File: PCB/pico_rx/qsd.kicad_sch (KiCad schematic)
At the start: 18 parts

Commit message: Update memory files, Update schematic
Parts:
- C? (x4): value 27n -> 15n
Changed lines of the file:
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@@
       (effects (font (size 1.27 1.27)))
     )
-    (property "Value" "27n" (at 176.276 143.51 90)
+    (property "Value" "15n" (at 176.276 143.51 90)
       (effects (font (size 1.27 1.27)))
     )
@@
       (effects (font (size 1.27 1.27)))
     )
-    (property "Value" "27n" (at 176.276 104.14 90)
+    (property "Value" "15n" (at 176.276 104.14 90)
       (effects (font (size 1.27 1.27)))
     )
@@
       (effects (font (size 1.27 1.27)))
     )
-    (property "Value" "27n" (at 166.116 143.51 90)
+    (property "Value" "15n" (at 166.116 143.51 90)
       (effects (font (size 1.27 1.27)))
     )
@@
       (effects (font (size 1.27 1.27)))
     )
-    (property "Value" "27n" (at 166.116 104.14 90)
-      (effects (font (size 1.27 1.27)))
-    )
+    (property "Value" "15n" (at 166.116 104.14 90)
+      (effects (font (size 1.27 1.27)))
+    )

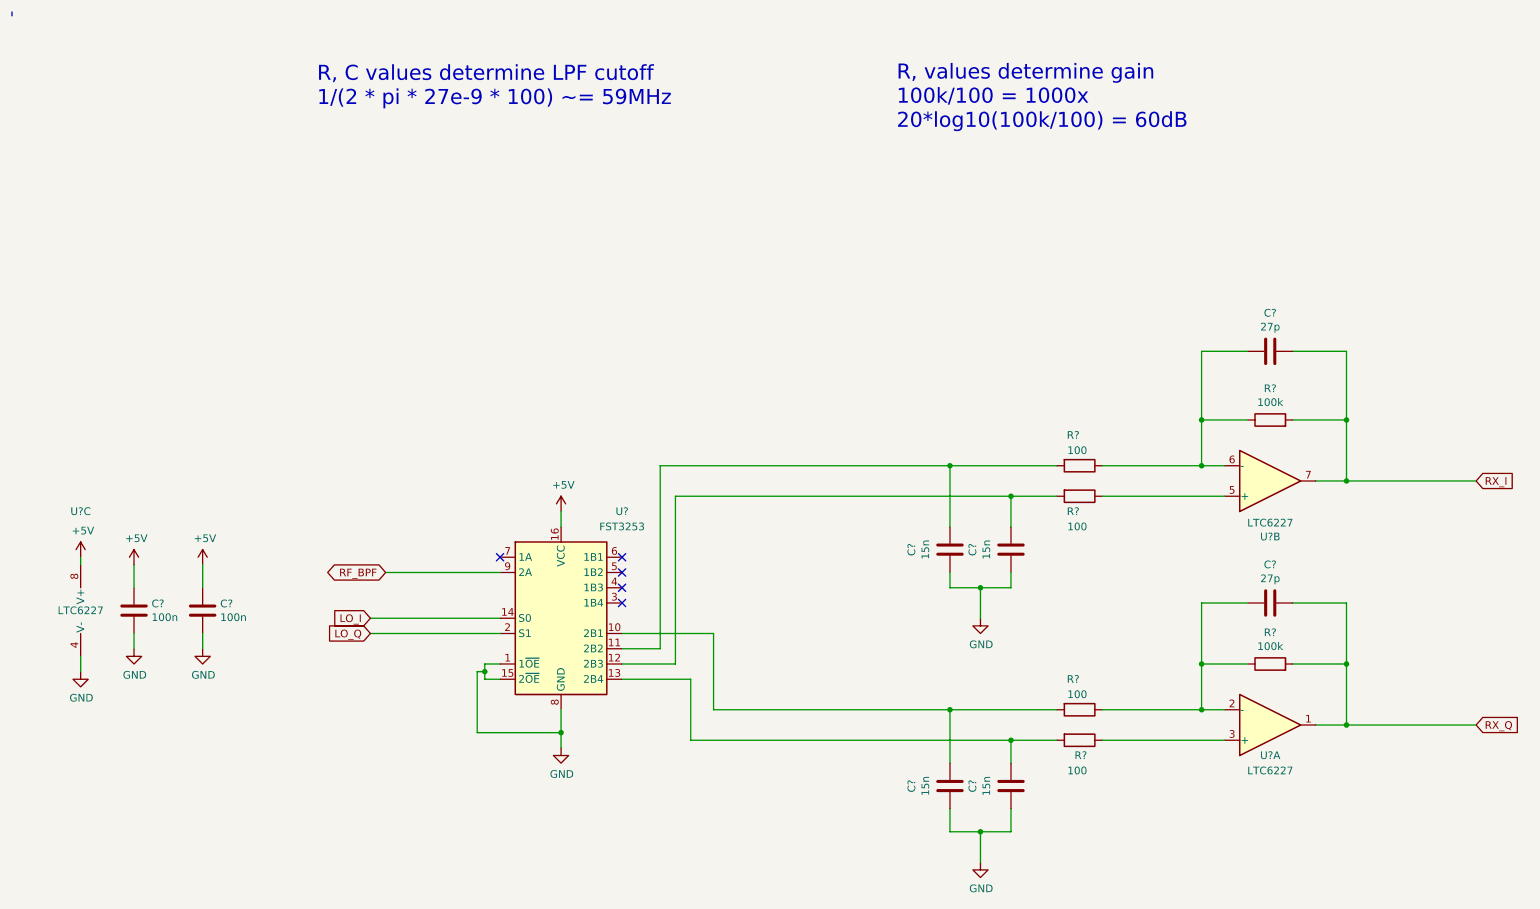
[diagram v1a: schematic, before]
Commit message: Correct error in schematic
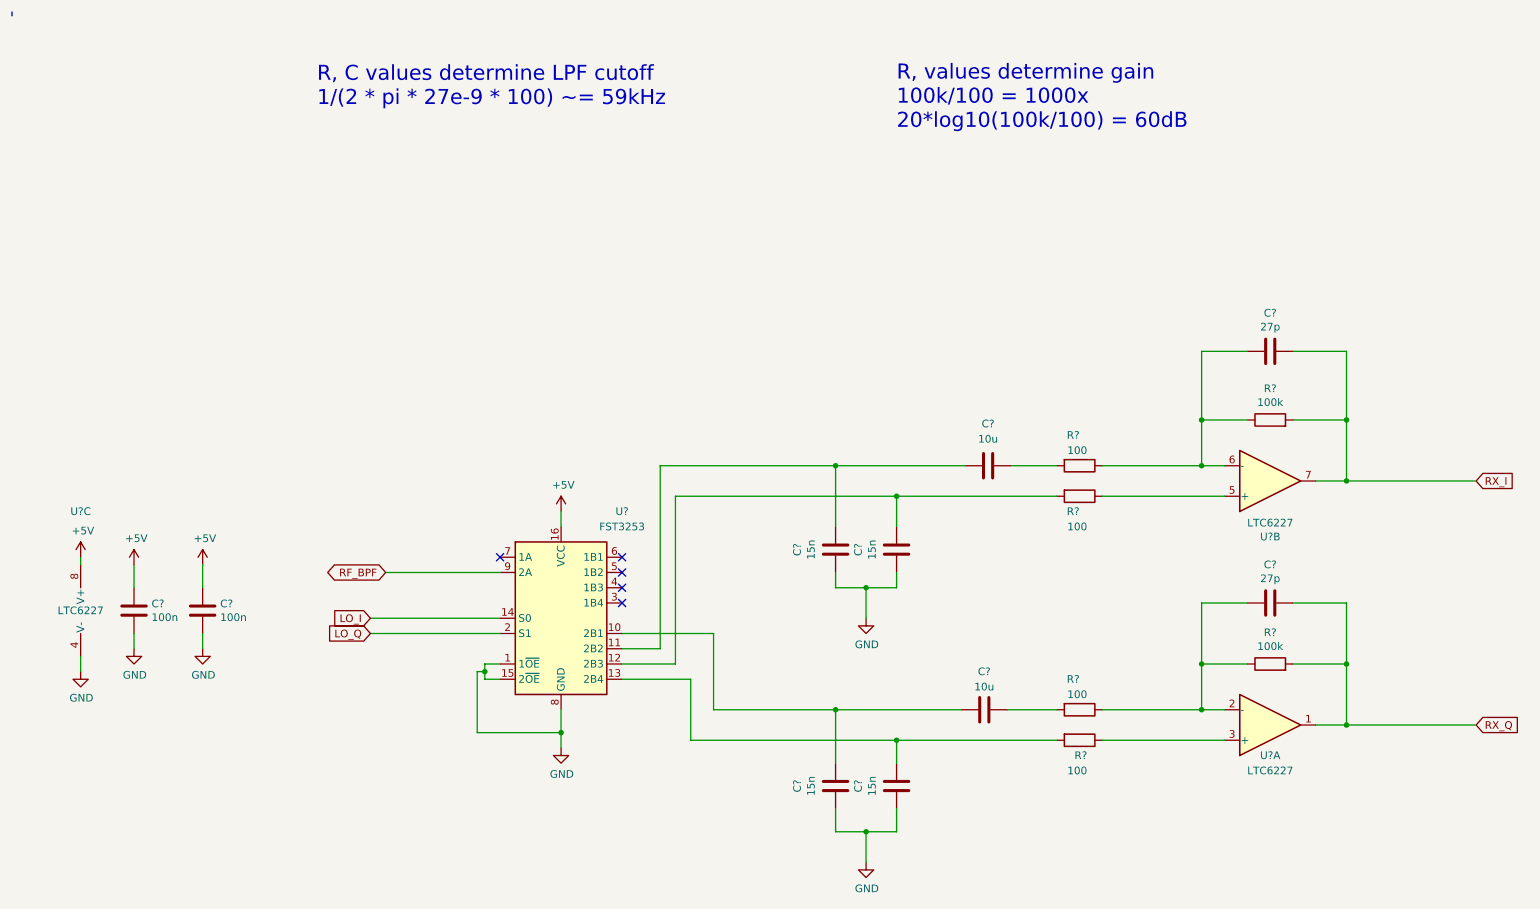
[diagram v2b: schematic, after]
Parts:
- added C? (x2): 10u, Capacitor_SMD:C_0805_2012Metric, symbol Device:C
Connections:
- net at C?.2, U?.10 (2B1): now also C?.2; no longer R?.2
- net at C?.2, U?.11 (2B2): now also C?.2; no longer R?.2
- new net: C?.1, R?.2 (x2)
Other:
- note added: "R, C values determine LPF cutoff 1/(2 * pi * 27e-9 * 100) ~= 59kHz"
- note removed: "R, C values determine LPF cutoff 1/(2 * pi * 27e-9 * 100) ~= 59MHz"
- moved on the sheet: C?

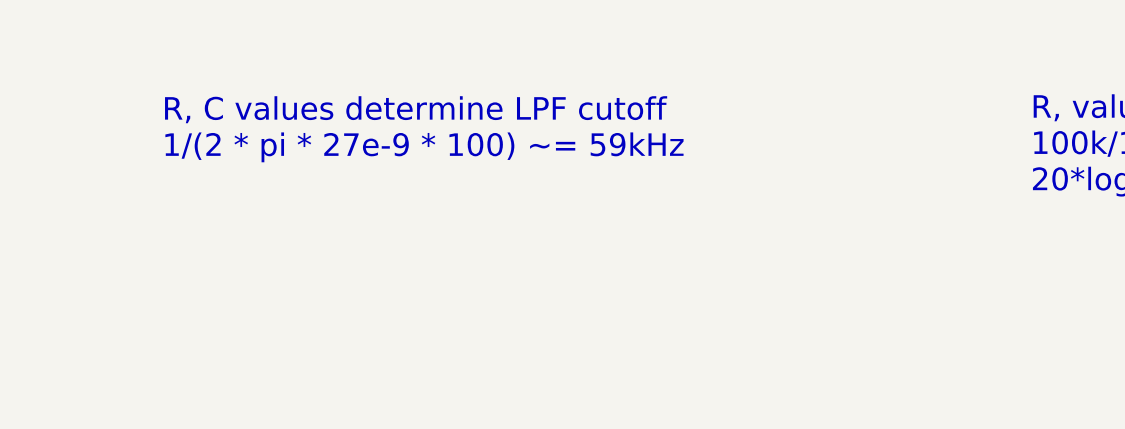
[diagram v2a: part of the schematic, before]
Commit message: Improve frequency resolution by making small adjustments to system clock. Add utility to upload memory contents over USB
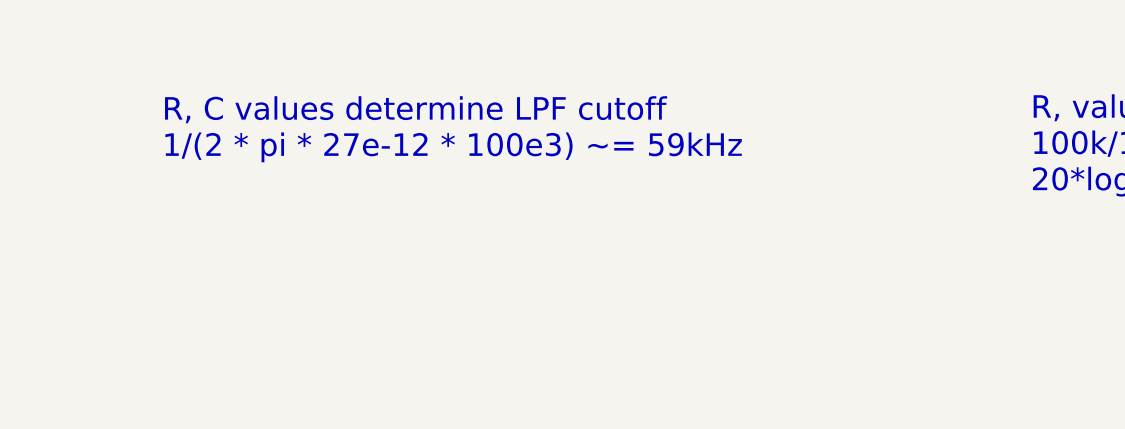
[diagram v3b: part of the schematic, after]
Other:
- note added: "R, C values determine LPF cutoff 1/(2 * pi * 27e-12 * 100e3) ~= 59kHz"
- note removed: "R, C values determine LPF cutoff 1/(2 * pi * 27e-9 * 100) ~= 59kHz"
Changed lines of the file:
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@@
     (effects (font (size 2.5 2.5)) (justify left bottom))
   )
-  (text "R, C values determine LPF cutoff\n1/(2 * pi * 27e-9 * 100) ~= 59kHz"
+  (text "R, C values determine LPF cutoff\n1/(2 * pi * 27e-12 * 100e3) ~= 59kHz"
     (at 64.77 30.48 0)
     (effects (font (size 2.5 2.5)) (justify left bottom))

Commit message: Update PCB design to fix issues found
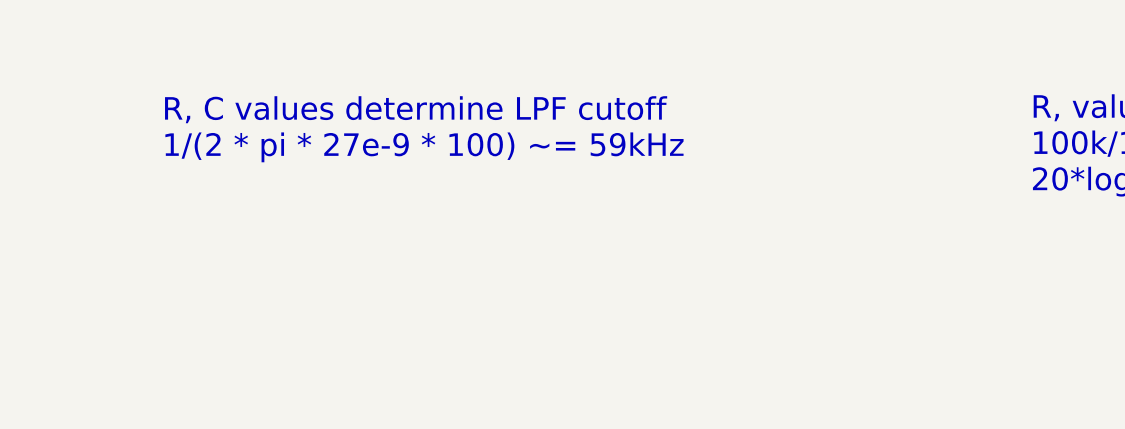
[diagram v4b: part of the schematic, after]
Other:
- note added: "R, C values determine LPF cutoff 1/(2 * pi * 27e-9 * 100) ~= 59kHz"
- note removed: "R, C values determine LPF cutoff 1/(2 * pi * 27e-12 * 100e3) ~= 59kHz"
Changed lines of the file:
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@@
     (effects (font (size 2.5 2.5)) (justify left bottom))
   )
-  (text "R, C values determine LPF cutoff\n1/(2 * pi * 27e-12 * 100e3) ~= 59kHz"
+  (text "R, C values determine LPF cutoff\n1/(2 * pi * 27e-9 * 100) ~= 59kHz"
     (at 64.77 30.48 0)
     (effects (font (size 2.5 2.5)) (justify left bottom))
